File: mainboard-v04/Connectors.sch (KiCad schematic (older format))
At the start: 18 parts, among them J1 503182-1852, J13 USB_C_Receptacle_USB2.0, J2 Conn_01x05, J3 Conn_01x01, J4 10118194-0001LF, U8 MR25H40MDF

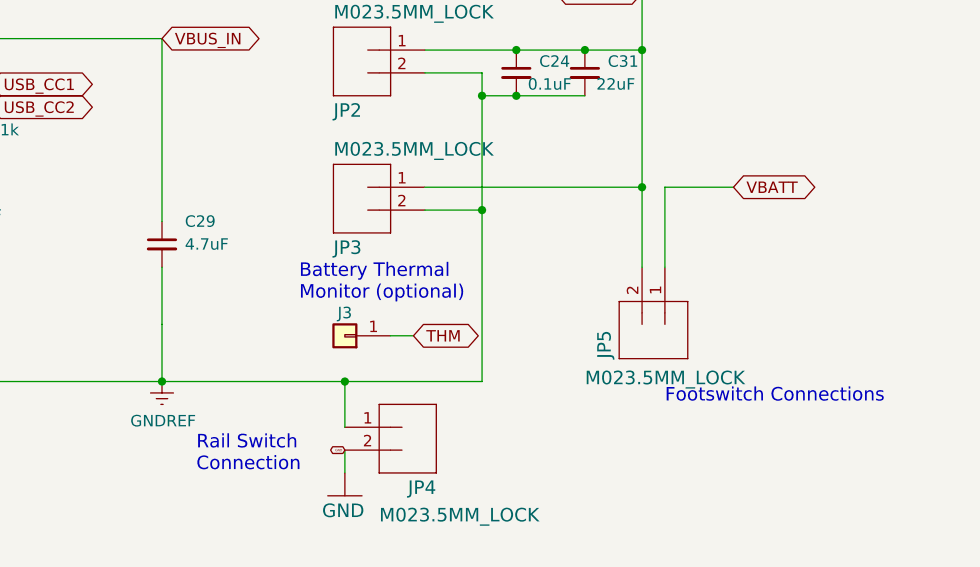
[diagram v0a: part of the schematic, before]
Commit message: adding mainbaordv04 layout and BOM
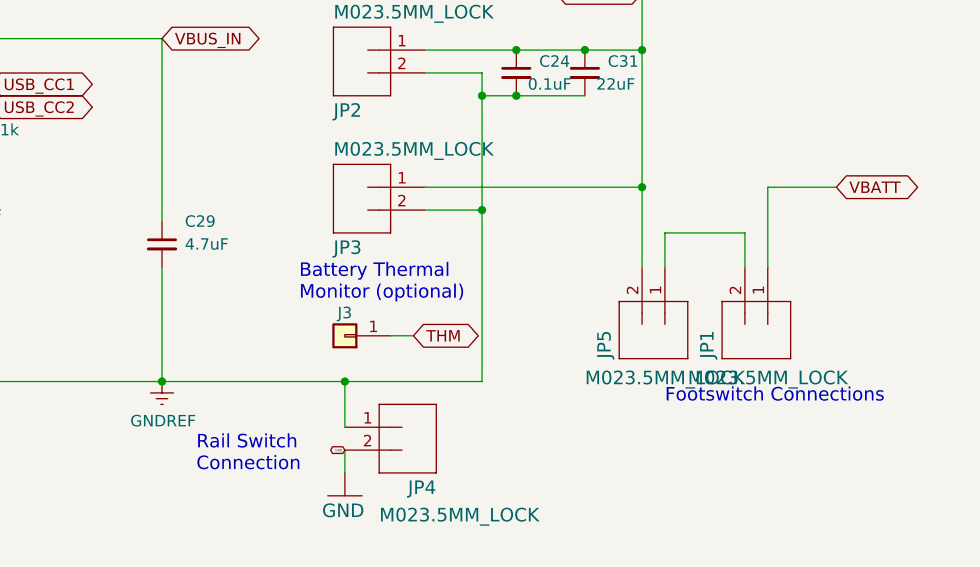
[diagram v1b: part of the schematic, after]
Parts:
- added JP1: M023.5MM_LOCK, mainboard:SCREWTERMINAL-3.5MM-2_LOCK, symbol mainboard:M023.5MM_LOCK
- U8: Flight (none) -> MR25H40MDF; Proto (none) -> W25Q80DVSNIG
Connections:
- net VBATT: now also JP1.1; no longer JP5.1
- new net: JP1.2, JP5.1
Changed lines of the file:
@@
 EESchema Schematic File Version 4
-LIBS:mainboard-cache
 EELAYER 30 0
 EELAYER END
@@
 Sheet 4 6
 Title "PyCubed Mainboard"
-Date "2019-11-27"
+Date "2020-01-08"
 Rev "v04"
-Comp "Stanford University"
+Comp ""
 Comment1 "Zac Manchester"
 Comment2 "Max Holliday"
@@
 GND
 Wire Wire Line
-	9250 3000 9250 2650
-Wire Wire Line
-	9250 2650 9550 2650
+	9700 3000 9700 2650
+Wire Wire Line
+	9700 2650 10000 2650
 Wire Wire Line
 	2300 1700 3000 1700
@@
 F 2 "mainboard:SON127P600X500X90-9N" H 1650 4700 50  0001 C CNN
 F 3 "" H 1650 4700 50  0001 C CNN
+F 4 "MR25H40MDF" H 1650 4700 50  0001 C CNN "Flight"
+F 5 "W25Q80DVSNIG" H 1650 4700 50  0001 C CNN "Proto"
 	1    1650 4700
 	1    0    0    -1
@@
 NoConn ~ 2300 2400
 NoConn ~ 2300 1400
-Text GLabel 9550 2650 2    50   BiDi ~ 0
+Text GLabel 10000 2650 2    50   BiDi ~ 0
 VBATT
 $Comp
@@
 	4850 3500 7050 3500
 Wire Wire Line
-	7050 3500 7050 3250
-Wire Wire Line
 	7050 2000 5450 2000
-Wire Wire Line
-	7050 3000 7050 3250
 $Comp
 L Device:C_Small C?
@@
 Wire Wire Line
 	7050 2000 7050 2800
+Wire Wire Line
+	7050 3000 7050 3500
+$Comp
+L mainboard:M023.5MM_LOCK JP?
+U 1 1 5DEA22AB
+P 9700 3300
+AR Path="/5DEA22AB" Ref="JP?"  Part="1"
+AR Path="/5CEC60EB/5DEA22AB" Ref="JP1"  Part="1"
+F 0 "JP1" H 9600 3530 59  0000 L BNN
+F 1 "M023.5MM_LOCK" V 9550 2950 59  0000 L BNN
+F 2 "mainboard:SCREWTERMINAL-3.5MM-2_LOCK" H 9700 3300 50  0001 C CNN
+F 3 "" H 9700 3300 50  0001 C CNN
+	1    9700 3300
+	0    -1   -1   0
+$EndComp
+Wire Wire Line
+	9600 3000 9600 2850
+Wire Wire Line
+	9600 2850 9250 2850
+Wire Wire Line
+	9250 2850 9250 3000
 $EndSCHEMATC

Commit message: cleaned up v04
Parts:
- J2: DNI (none) -> DNI
- JP1, JP2, JP3, JP4, JP5: value M023.5MM_LOCK -> 1985807
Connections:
- net xSDCS renamed SD_CS
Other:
- note added: "NOTE: Components labeled "do not install" (DNI) are not populated by default"
- moved on the sheet: J3
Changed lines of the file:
@@
 EELAYER 30 0
 EELAYER END
-$Descr User 11693 8851
+$Descr A4 11693 8268
 encoding utf-8
-Sheet 4 6
+Sheet 3 6
 Title "PyCubed Mainboard"
-Date "2020-01-08"
+Date "2020-02-10"
 Rev "v04"
-Comp ""
-Comment1 "Zac Manchester"
-Comment2 "Max Holliday"
+Comp "Max Holliday"
+Comment1 ""
+Comment2 ""
 Comment3 ""
 Comment4 ""
@@
 	2300 1500 2550 1500
 Text GLabel 2600 1500 2    50   BiDi ~ 0
-xSDCS
+SD_CS
 Wire Wire Line
 	8450 2750 8200 2750
@@
 AR Path="/1D5F55F3" Ref="JP?"  Part="1"
 AR Path="/5CEC60EB/1D5F55F3" Ref="JP2"  Part="1"
-F 0 "JP2" H 7800 2280 59  0000 L BNN
-F 1 "M023.5MM_LOCK" H 7800 1850 59  0000 L BNN
+F 0 "JP2" H 7600 2050 59  0000 L BNN
+F 1 "1985807" H 7400 2150 59  0000 L BNN
 F 2 "mainboard:SCREWTERMINAL-3.5MM-2_LOCK" H 7900 2050 50  0001 C CNN
 F 3 "" H 7900 2050 50  0001 C CNN
@@
 AR Path="/55623696" Ref="JP?"  Part="1"
 AR Path="/5CEC60EB/55623696" Ref="JP3"  Part="1"
-F 0 "JP3" H 7800 2880 59  0000 L BNN
-F 1 "M023.5MM_LOCK" H 7800 2450 59  0000 L BNN
+F 0 "JP3" H 7600 2600 59  0000 L BNN
+F 1 "1985807" H 7400 2700 59  0000 L BNN
 F 2 "mainboard:SCREWTERMINAL-3.5MM-2_LOCK" H 7900 2650 50  0001 C CNN
 F 3 "" H 7900 2650 50  0001 C CNN
@@
 AR Path="/6F37A4EE" Ref="JP?"  Part="1"
 AR Path="/5CEC60EB/6F37A4EE" Ref="JP5"  Part="1"
-F 0 "JP5" H 9150 3530 59  0000 L BNN
-F 1 "M023.5MM_LOCK" V 9100 2950 59  0000 L BNN
+F 0 "JP5" V 9350 3550 59  0000 L BNN
+F 1 "1985807" V 9250 3500 59  0000 L BNN
 F 2 "mainboard:SCREWTERMINAL-3.5MM-2_LOCK" H 9250 3300 50  0001 C CNN
 F 3 "" H 9250 3300 50  0001 C CNN
@@
 	1    0    0    -1
 $EndComp
-Text Notes 9250 3600 0    59   ~ 0
+Text Notes 8950 3700 0    59   ~ 0
 Footswitch Connections
 Text Notes 7850 1700 0    85   ~ 0
@@
 F 2 "Connector_PinHeader_2.54mm:PinHeader_1x05_P2.54mm_Vertical" H 2750 6650 50  0001 C CNN
 F 3 "~" H 2750 6650 50  0001 C CNN
+F 4 "DNI" H 2900 6650 50  0000 C CNB "DNI"
 	1    2750 6650
 	1    0    0    -1
@@
 Wire Wire Line
 	1500 4900 1650 4900
-Text Notes 8550 7550 0    200  ~ 0
+Text Notes 8550 6950 0    200  ~ 40
 Connectors
 NoConn ~ 2300 2100
@@
 AR Path="/EDD14CA3" Ref="JP?"  Part="1"
 AR Path="/5CEC60EB/EDD14CA3" Ref="JP4"  Part="1"
-F 0 "JP4" H 8050 3930 59  0000 L BNN
-F 1 "M023.5MM_LOCK" H 7600 4050 59  0000 L BNN
+F 0 "JP4" H 7850 3650 59  0000 L BNN
+F 1 "1985807" H 7600 3750 59  0000 L BNN
 F 2 "mainboard:SCREWTERMINAL-3.5MM-2_LOCK" H 8150 3700 50  0001 C CNN
 F 3 "" H 8150 3700 50  0001 C CNN
@@
 Wire Wire Line
 	8450 3500 8450 2750
-Text Notes 7650 3150 0    59   ~ 0
+Text Notes 7500 3200 0    59   ~ 0
 Battery Thermal \nMonitor (optional)
 $Comp
 L Connector_Generic:Conn_01x01 J3
 U 1 1 5DECAB53
-P 7850 3300
-F 0 "J3" H 7850 3200 50  0000 C CNN
-F 1 "Conn_01x01" H 8150 3300 50  0001 C CNN
-F 2 "Connector_PinHeader_2.54mm:PinHeader_1x01_P2.54mm_Vertical" H 7850 3300 50  0001 C CNN
-F 3 "~" H 7850 3300 50  0001 C CNN
-	1    7850 3300
+P 7800 3350
+F 0 "J3" H 7800 3250 50  0000 C CNN
+F 1 "Conn_01x01" H 8100 3350 50  0001 C CNN
+F 2 "Connector_PinHeader_2.54mm:PinHeader_1x01_P2.54mm_Vertical" H 7800 3350 50  0001 C CNN
+F 3 "~" H 7800 3350 50  0001 C CNN
+	1    7800 3350
 	-1   0    0    1
 $EndComp
-Text GLabel 8150 3300 2    50   BiDi ~ 0
+Text GLabel 8100 3350 2    50   BiDi ~ 0
 THM
 Wire Wire Line
-	8050 3300 8150 3300
+	8000 3350 8100 3350
 Connection ~ 7850 3500
 Wire Wire Line
@@
 F 4 "Micro Usb, 2.0 Type b, Rcpt, Smt" H 4600 4050 50  0001 L BNN "Field4"
 F 5 "10118194-0001LF" H 4600 4050 50  0001 L BNN "Field5"
-F 6 "DNI" H 4800 4000 50  0000 C CNN "DNI"
+F 6 "DNI" H 4800 4000 50  0000 C CNB "DNI"
 	1    4600 4050
 	-1   0    0    -1
@@
 AR Path="/5DEA22AB" Ref="JP?"  Part="1"
 AR Path="/5CEC60EB/5DEA22AB" Ref="JP1"  Part="1"
-F 0 "JP1" H 9600 3530 59  0000 L BNN
-F 1 "M023.5MM_LOCK" V 9550 2950 59  0000 L BNN
+F 0 "JP1" V 9800 3000 59  0000 L BNN
+F 1 "1985807" V 9700 2800 59  0000 L BNN
 F 2 "mainboard:SCREWTERMINAL-3.5MM-2_LOCK" H 9700 3300 50  0001 C CNN
 F 3 "" H 9700 3300 50  0001 C CNN
@@
 Wire Wire Line
 	9250 2850 9250 3000
+Text Notes 7000 6500 0    65   ~ 0
+NOTE: Components labeled "do not install" (DNI) are not populated by default
+Wire Notes Line
+	6950 6500 6950 6400
+Wire Notes Line
+	6950 6400 11200 6400
 $EndSCHEMATC
